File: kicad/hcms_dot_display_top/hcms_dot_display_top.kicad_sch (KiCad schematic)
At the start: 56 parts, among them J1 Conn_01x12, J2 USB_C_Receptacle_USB2.0, J3 Conn_01x12, J4 Conn_01x11_Female, J5 Conn_01x11_Male, J6 Conn_01x12, J7 Conn_01x12, J8 Conn_01x02_Male, Q1 Q_PMOS_DSG, Q2 Q_PMOS_DSG, Q3 Q_PMOS_DSG, Q4 Q_PMOS_DSG, Q5 Q_PMOS_DSG, Q6 Q_PMOS_DSG, SW1 SW_DIP_x03, U1 ATtiny1626-X, U2 FT231XS

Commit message: Top board refined
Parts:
- removed C1, C9: 10nF, Capacitor_SMD:C_0603_1608Metric, symbol Device:C_Small
- removed C12, C2, C6, C8: 100nF, Capacitor_SMD:C_0603_1608Metric, symbol Device:C_Small
- removed C4, C5: 47pF, Capacitor_SMD:C_0603_1608Metric, symbol Device:C_Small
- removed C7: 4.7uF, Capacitor_SMD:C_0603_1608Metric, symbol Device:C_Small
- removed J2: USB_C_Receptacle_USB2.0, hcms:213716-0001, symbol Connector:USB_C_Receptacle_USB2.0
- removed J4: Conn_01x11_Female, Connector_PinSocket_2.54mm:PinSocket_1x11_P2.54mm_Vertical, symbol Connector:Conn_01x11_Female
- removed J8: Conn_01x02_Male, Connector_PinHeader_2.54mm:PinHeader_1x02_P2.54mm_Vertical, symbol Connector:Conn_01x02_Male
- removed MH1, MH2: MountingHole, MountingHole:MountingHole_2.2mm_M2_Pad_Via, symbol Mechanical:MountingHole
- removed Q6: Q_PMOS_DSG, Package_SO:SO-8_5.3x6.2mm_P1.27mm, symbol hcms_dot_display:SI4425FDY
- removed R15: 1k, Resistor_SMD:R_0603_1608Metric, symbol Device:R
- removed R18, R19, R20: 10k, Resistor_SMD:R_0603_1608Metric, symbol Device:R
- removed R21, R22, R23: 0, Resistor_SMD:R_0603_1608Metric, symbol Device:R
- removed R3: 200, Resistor_SMD:R_0603_1608Metric, symbol Device:R
- removed R4, R5: 5.1k, Resistor_SMD:R_0603_1608Metric, symbol Device:R
- removed R8, R9: 27, Resistor_SMD:R_0603_1608Metric, symbol Device:R
- removed RV1: R_Potentiometer, hcms:TRIM_3352T-1-201LF, symbol Device:R_Potentiometer
- removed SW1: SW_DIP_x03, hcms:BPA03SB, symbol Switch:SW_DIP_x03
- removed U1: ATtiny1626-X, Package_SO:SSOP-20_5.3x7.2mm_P0.65mm, symbol hcms_dot_display:ATtiny826-SXX
- removed U2: FT231XS, Package_SO:SSOP-20_3.9x8.7mm_P0.635mm, symbol Interface_USB:FT231XS
- renumbered J5 to J4
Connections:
- no-connect marks 24 -> 8
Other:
- note removed: "3V3 generated from chip internal LDO, can only source 50mA"
- note removed: "BOTTOM PCB"
- note removed: "Backup power connection"
- note removed: "DMN2046U"
- note removed: "MIC5018YM4-TR"
- note removed: "PWM available on pins connected to TCA or TCB, refer to I/O mux table 3-1 PA3 and PA5 connected to both TCA and TCB"
- note removed: "SI4425FDY-T1-GE3"
- moved on the sheet: C10, C11, C3, D1A, D1B, J1, J3, J4, J6, J7, Q1, Q2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

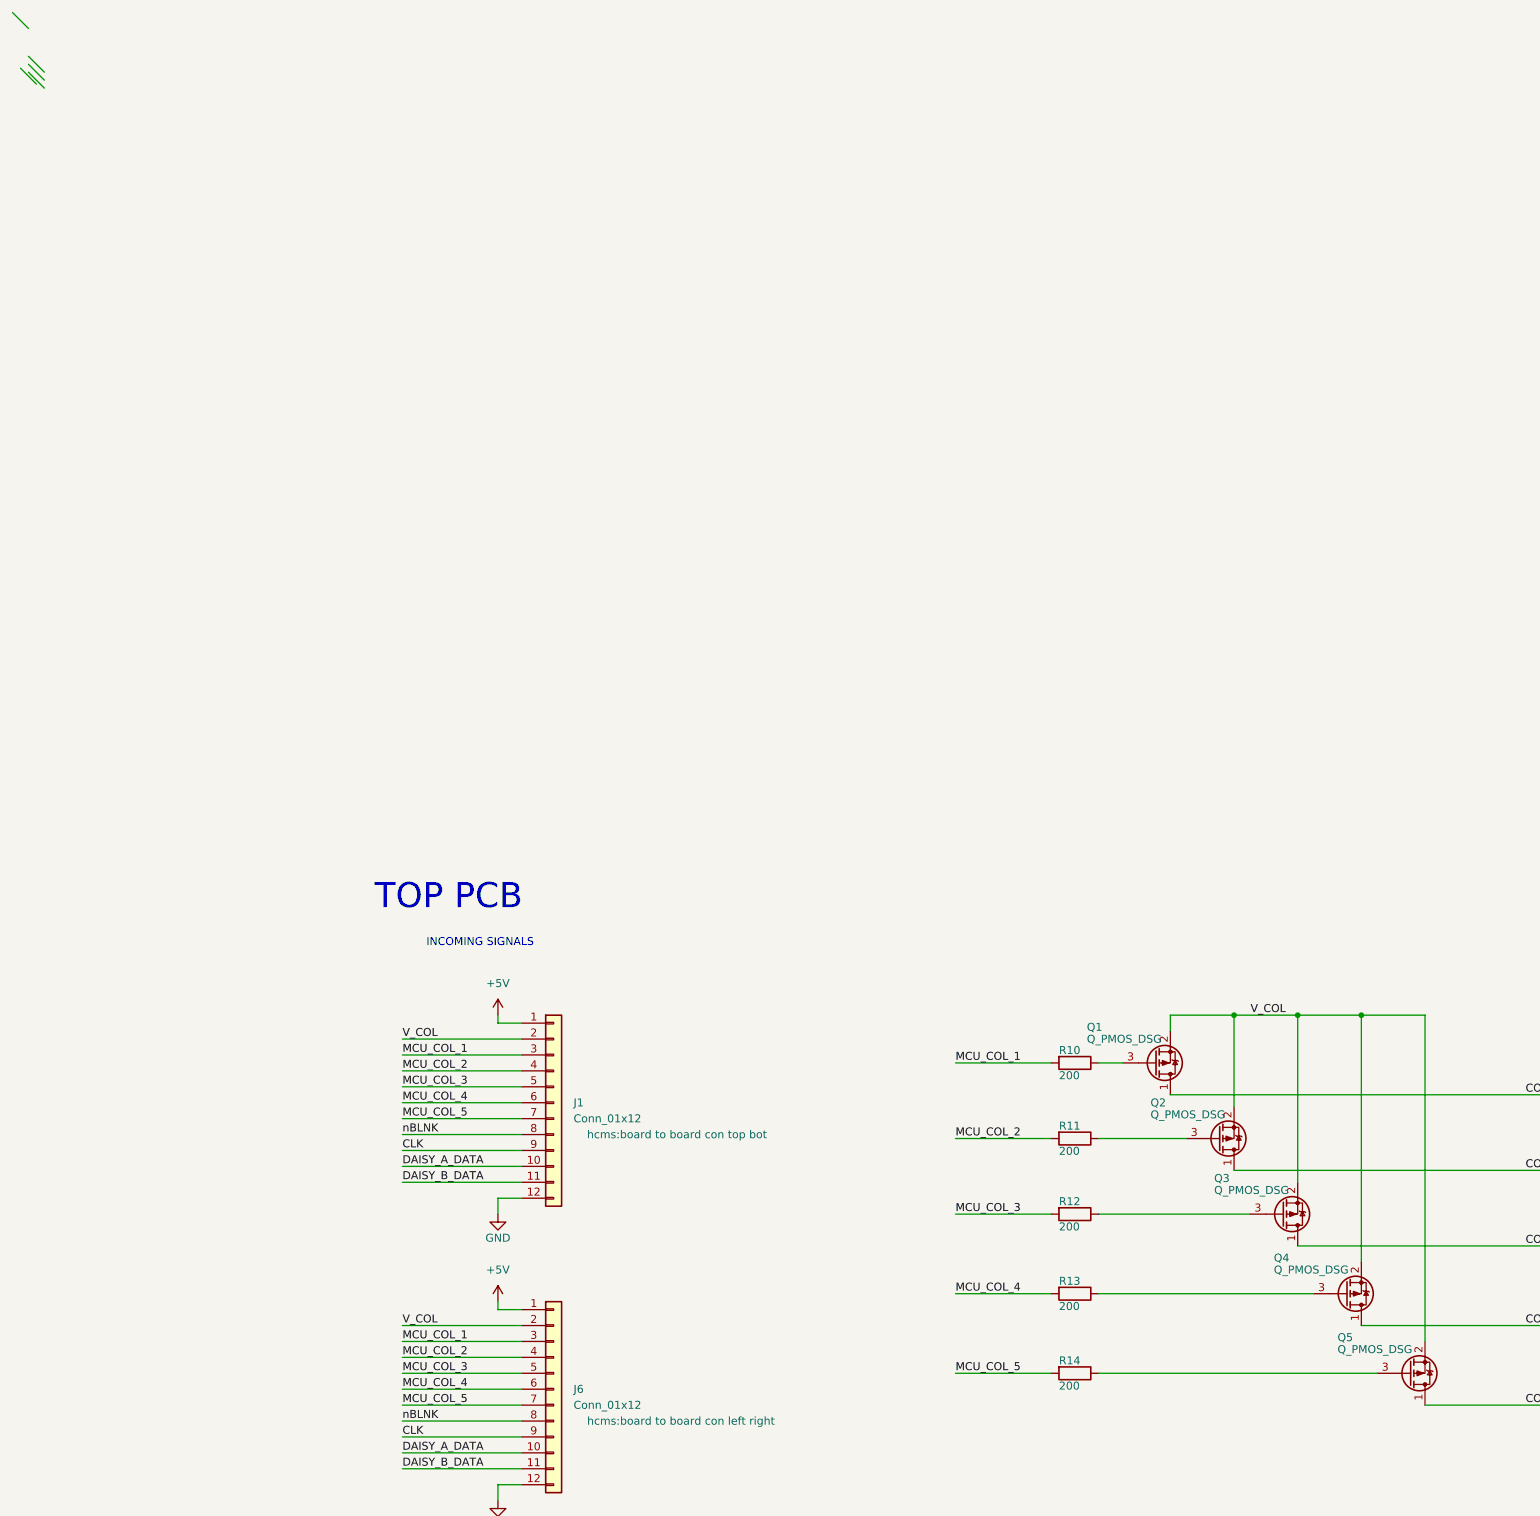
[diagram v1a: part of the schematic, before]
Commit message: Updated DMP footprint on bottom board and re routed
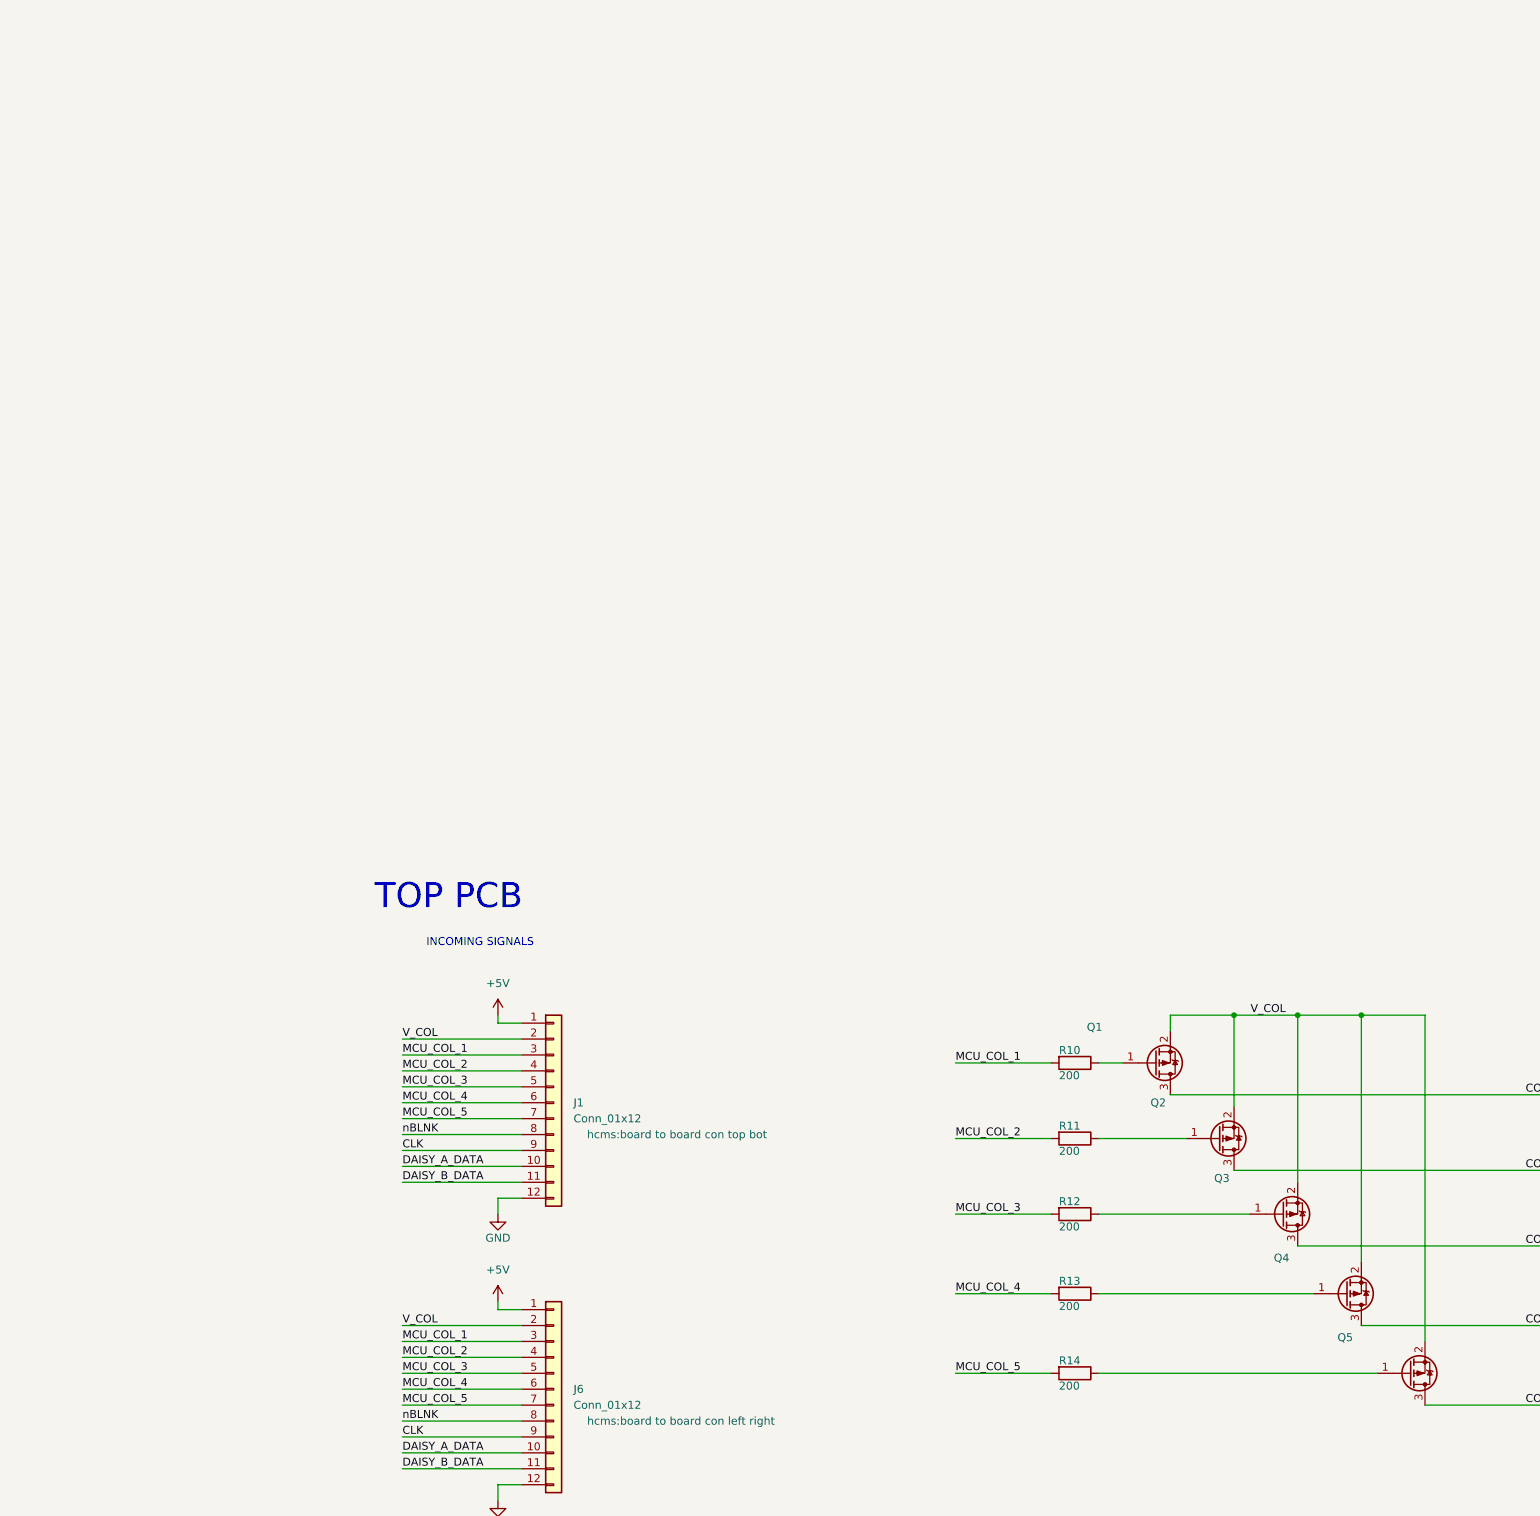
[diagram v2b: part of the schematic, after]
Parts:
- Q1, Q2, Q3, Q4, Q5: value Q_PMOS_DSG -> (none); footprint Package_TO_SOT_SMD:SOT-23 -> (none); symbol Device:Q_PMOS_DSG -> Device:Q_PMOS_GSD
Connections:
- net COL_1: now also Q1.3 (D); no longer Q1.1 (D)
- net COL_2: now also Q2.3 (D); no longer Q2.1 (D)
- net COL_3: now also Q3.3 (D); no longer Q3.1 (D)
- net COL_4: now also Q4.3 (D); no longer Q4.1 (D)
- net COL_5: now also Q5.3 (D); no longer Q5.1 (D)
- net at R10.1: now also Q1.1 (G); no longer Q1.3 (G)
- net at R13.1: now also Q4.1 (G); no longer Q4.3 (G)
- net at R14.1: now also Q5.1 (G); no longer Q5.3 (G)
- net at R11.1: now also Q2.1 (G); no longer Q2.3 (G)
- net at R12.1: now also Q3.1 (G); no longer Q3.3 (G)
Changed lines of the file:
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@@
   (no_connect (at 288.925 107.95))
   (no_connect (at 288.925 105.41))
-  (bus_entry (at -35.56 -45.72) (size 2.54 2.54)
-    (stroke (width 0) (type default) (color 0 0 0 0))
-  )
-  (bus_entry (at -35.56 -46.99) (size 2.54 2.54)
-    (stroke (width 0) (type default) (color 0 0 0 0))
-  )
-  (bus_entry (at -36.83 -46.355) (size 2.54 2.54)
-    (stroke (width 0) (type default) (color 0 0 0 0))
-  )
-  (bus_entry (at -38.1 -55.245) (size 2.54 2.54)
-    (stroke (width 0) (type default) (color 0 0 0 0))
-  )
-  (bus_entry (at -35.56 -48.26) (size 2.54 2.54)
-    (stroke (width 0) (type default) (color 0 0 0 0))
-  )
   (wire (pts (xy 289.56 173.99) (xy 302.26 173.99))
     (stroke (width 0) (type default) (color 0 0 0 0))
@@
     (pin "9B")
   )
-  (symbol (lib_id "Device:Q_PMOS_DSG") (at 154.305 124.46 0) (mirror x) (unit 1)
+  (symbol (lib_id "Device:Q_PMOS_GSD") (at 154.305 124.46 0) (mirror x) (unit 1)
     (in_bom yes) (on_board yes)
     (property "Reference" "Q2" (id 0) (at 143.51 118.745 0)
       (effects (font (size 1.27 1.27)) (justify left))
     )
-    (property "Value" "Q_PMOS_DSG" (id 1) (at 143.51 120.65 0)
-      (effects (font (size 1.27 1.27)) (justify left))
-    )
-    (property "Footprint" "Package_TO_SOT_SMD:SOT-23" (id 2) (at 159.385 127 0)
+    (property "Value" "" (id 1) (at 143.51 120.65 0)
+      (effects (font (size 1.27 1.27)) (justify left))
+    )
+    (property "Footprint" "" (id 2) (at 159.385 127 0)
       (effects (font (size 1.27 1.27)) hide)
     )
@@
     (pin "1")
   )
-  (symbol (lib_id "Device:Q_PMOS_DSG") (at 144.145 112.395 0) (mirror x) (unit 1)
+  (symbol (lib_id "Device:Q_PMOS_GSD") (at 144.145 112.395 0) (mirror x) (unit 1)
     (in_bom yes) (on_board yes)
     (property "Reference" "Q1" (id 0) (at 133.35 106.68 0)
       (effects (font (size 1.27 1.27)) (justify left))
     )
-    (property "Value" "Q_PMOS_DSG" (id 1) (at 133.35 108.585 0)
-      (effects (font (size 1.27 1.27)) (justify left))
-    )
-    (property "Footprint" "Package_TO_SOT_SMD:SOT-23" (id 2) (at 149.225 114.935 0)
+    (property "Value" "" (id 1) (at 133.35 108.585 0)
+      (effects (font (size 1.27 1.27)) (justify left))
+    )
+    (property "Footprint" "" (id 2) (at 149.225 114.935 0)
       (effects (font (size 1.27 1.27)) hide)
     )
@@
     (pin "9")
   )
-  (symbol (lib_id "Device:Q_PMOS_DSG") (at 184.785 161.925 0) (mirror x) (unit 1)
+  (symbol (lib_id "Device:Q_PMOS_GSD") (at 184.785 161.925 0) (mirror x) (unit 1)
     (in_bom yes) (on_board yes)
     (property "Reference" "Q5" (id 0) (at 173.355 156.21 0)
       (effects (font (size 1.27 1.27)) (justify left))
     )
-    (property "Value" "Q_PMOS_DSG" (id 1) (at 173.355 158.115 0)
-      (effects (font (size 1.27 1.27)) (justify left))
-    )
-    (property "Footprint" "Package_TO_SOT_SMD:SOT-23" (id 2) (at 189.865 164.465 0)
+    (property "Value" "" (id 1) (at 173.355 158.115 0)
+      (effects (font (size 1.27 1.27)) (justify left))
+    )
+    (property "Footprint" "" (id 2) (at 189.865 164.465 0)
       (effects (font (size 1.27 1.27)) hide)
     )
@@
     (pin "2")
   )
-  (symbol (lib_id "Device:Q_PMOS_DSG") (at 164.465 136.525 0) (mirror x) (unit 1)
+  (symbol (lib_id "Device:Q_PMOS_GSD") (at 164.465 136.525 0) (mirror x) (unit 1)
     (in_bom yes) (on_board yes)
     (property "Reference" "Q3" (id 0) (at 153.67 130.81 0)
       (effects (font (size 1.27 1.27)) (justify left))
     )
-    (property "Value" "Q_PMOS_DSG" (id 1) (at 153.67 132.715 0)
-      (effects (font (size 1.27 1.27)) (justify left))
-    )
-    (property "Footprint" "Package_TO_SOT_SMD:SOT-23" (id 2) (at 169.545 139.065 0)
+    (property "Value" "" (id 1) (at 153.67 132.715 0)
+      (effects (font (size 1.27 1.27)) (justify left))
+    )
+    (property "Footprint" "" (id 2) (at 169.545 139.065 0)
       (effects (font (size 1.27 1.27)) hide)
     )
@@
     (pin "2")
   )
-  (symbol (lib_id "Device:Q_PMOS_DSG") (at 174.625 149.225 0) (mirror x) (unit 1)
+  (symbol (lib_id "Device:Q_PMOS_GSD") (at 174.625 149.225 0) (mirror x) (unit 1)
     (in_bom yes) (on_board yes)
     (property "Reference" "Q4" (id 0) (at 163.195 143.51 0)
       (effects (font (size 1.27 1.27)) (justify left))
     )
-    (property "Value" "Q_PMOS_DSG" (id 1) (at 163.195 145.415 0)
-      (effects (font (size 1.27 1.27)) (justify left))
-    )
-    (property "Footprint" "Package_TO_SOT_SMD:SOT-23" (id 2) (at 179.705 151.765 0)
+    (property "Value" "" (id 1) (at 163.195 145.415 0)
+      (effects (font (size 1.27 1.27)) (justify left))
+    )
+    (property "Footprint" "" (id 2) (at 179.705 151.765 0)
       (effects (font (size 1.27 1.27)) hide)
     )
@@
     )
     (path "/cb19c6f6-ba2e-40c5-b24e-87d5c3df300e"
-      (reference "Q1") (unit 1) (value "Q_PMOS_DSG") (footprint "Package_TO_SOT_SMD:SOT-23")
+      (reference "Q1") (unit 1) (value "Q_PMOS_GSD") (footprint "Package_TO_SOT_SMD:SOT-23")
     )
     (path "/c1d65eb9-d436-4504-85a2-7f4225a92715"
-      (reference "Q2") (unit 1) (value "Q_PMOS_DSG") (footprint "Package_TO_SOT_SMD:SOT-23")
+      (reference "Q2") (unit 1) (value "Q_PMOS_GSD") (footprint "Package_TO_SOT_SMD:SOT-23")
     )
     (path "/edddec30-3505-4a33-b43d-e5bc5c295d58"
-      (reference "Q3") (unit 1) (value "Q_PMOS_DSG") (footprint "Package_TO_SOT_SMD:SOT-23")
+      (reference "Q3") (unit 1) (value "Q_PMOS_GSD") (footprint "Package_TO_SOT_SMD:SOT-23")
     )
     (path "/f377543d-c04d-4e23-aa87-7188a3ea31c8"
-      (reference "Q4") (unit 1) (value "Q_PMOS_DSG") (footprint "Package_TO_SOT_SMD:SOT-23")
+      (reference "Q4") (unit 1) (value "Q_PMOS_GSD") (footprint "Package_TO_SOT_SMD:SOT-23")
     )
     (path "/d485ba26-cbd0-4449-8b86-d68adf22852b"
-      (reference "Q5") (unit 1) (value "Q_PMOS_DSG") (footprint "Package_TO_SOT_SMD:SOT-23")
+      (reference "Q5") (unit 1) (value "Q_PMOS_GSD") (footprint "Package_TO_SOT_SMD:SOT-23")
     )
     (path "/0342ce35-bc04-43c5-9d8e-7e0b77b32d15"
